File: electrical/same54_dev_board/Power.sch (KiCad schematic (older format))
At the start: 1 part, among them U1 p_ATSAME54P20A-AU

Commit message: Trying to figure out how I want to do power...
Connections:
- net at U1.14 (GNDANA1): now also U1.25 (GNDANA2)
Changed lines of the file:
@@
 Wire Wire Line
 	5800 3450 5800 3550
+Wire Wire Line
+	5800 3800 5800 3900
 $EndSCHEMATC

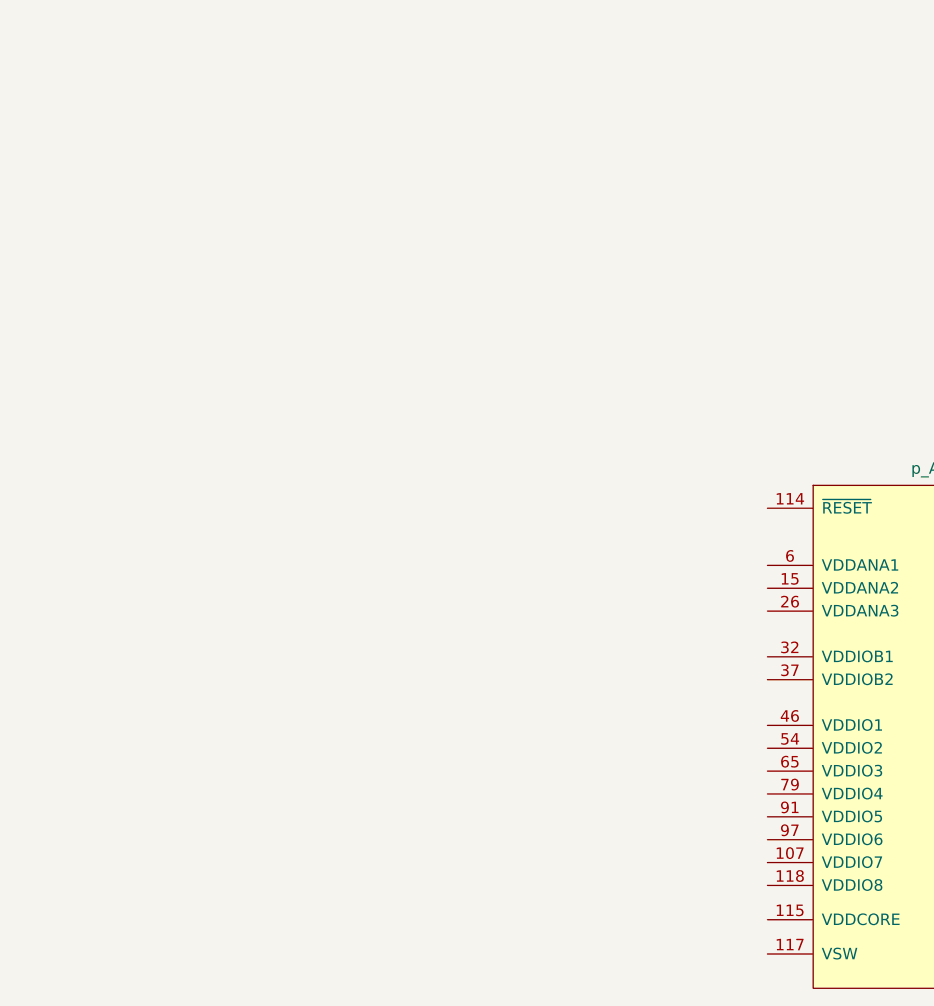
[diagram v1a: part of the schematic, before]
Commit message: going with barrel jack 5v+2A optional input, with usb supplying 400mA + 100mA for internals
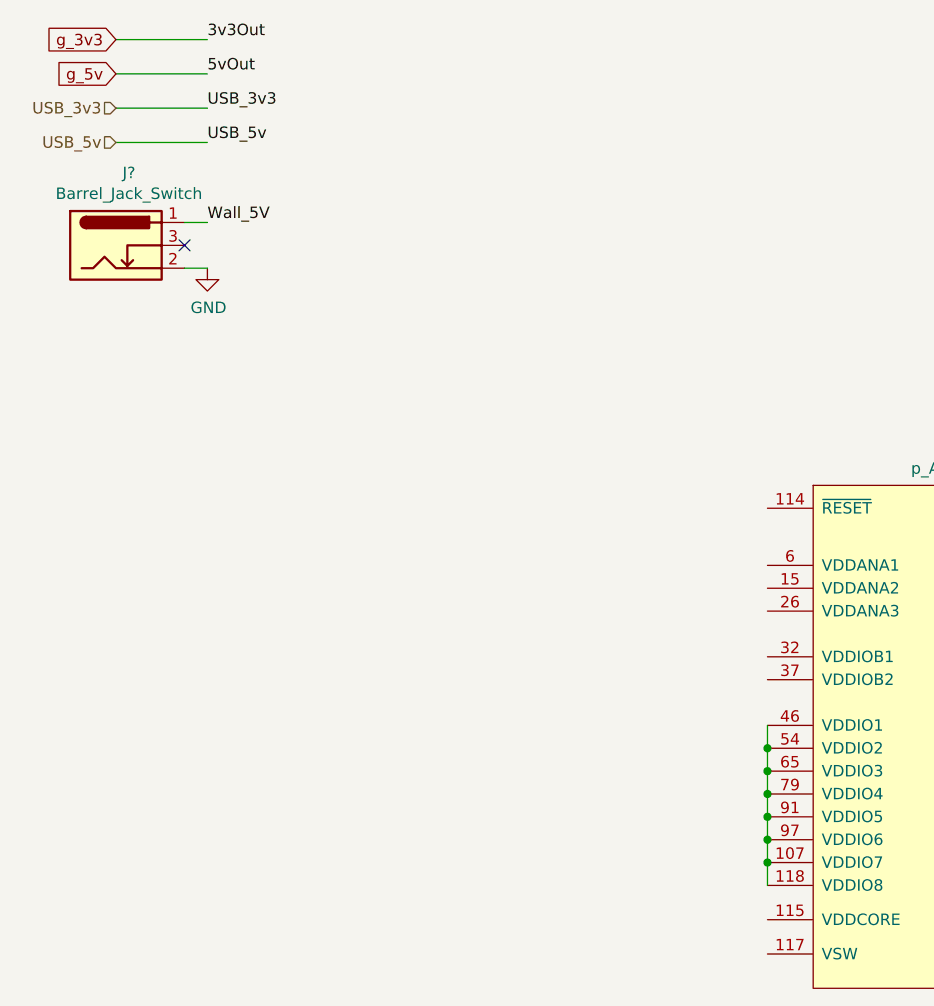
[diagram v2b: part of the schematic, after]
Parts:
- added J?: Barrel_Jack_Switch, symbol Connector:Barrel_Jack_Switch
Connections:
- net at U1.107 (VDDIO7): now also U1.118 (VDDIO8), U1.46 (VDDIO1), U1.54 (VDDIO2), U1.65 (VDDIO3), U1.79 (VDDIO4), U1.91 (VDDIO5), U1.97 (VDDIO6)
- new net GND: J?.2
- new net Wall_5V: J?.1
- no-connect marks 0 -> 1
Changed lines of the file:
@@
 Wire Wire Line
 	5800 3800 5800 3900
+Text HLabel 950  900  0    50   Input ~ 0
+USB_3v3
+Text HLabel 950  1050 0    50   Input ~ 0
+USB_5v
+Text GLabel 950  600  0    50   Input ~ 0
+g_3v3
+Text GLabel 950  750  0    50   Input ~ 0
+g_5v
+Wire Wire Line
+	950  900  1350 900
+Text Label 1350 900  0    50   ~ 0
+USB_3v3
+Wire Wire Line
+	950  1050 1350 1050
+Text Label 1350 1050 0    50   ~ 0
+USB_5v
+Wire Wire Line
+	950  600  1350 600
+Wire Wire Line
+	950  750  1350 750
+Text Label 1350 600  0    50   ~ 0
+3v3Out
+Text Label 1350 750  0    50   ~ 0
+5vOut
+Wire Wire Line
+	3800 3600 3800 3700
+Connection ~ 3800 3700
+Wire Wire Line
+	3800 3700 3800 3800
+Connection ~ 3800 3800
+Wire Wire Line
+	3800 3800 3800 3900
+Connection ~ 3800 3900
+Wire Wire Line
+	3800 3900 3800 4000
+Connection ~ 3800 4000
+Wire Wire Line
+	3800 4000 3800 4100
+Connection ~ 3800 4100
+Wire Wire Line
+	3800 4100 3800 4200
+Connection ~ 3800 4200
+Wire Wire Line
+	3800 4200 3800 4300
+$Comp
+L Connector:Barrel_Jack_Switch J?
+U 1 1 5E88DD8C
+P 950 1500
+F 0 "J?" H 1007 1817 50  0000 C CNN
+F 1 "Barrel_Jack_Switch" H 1007 1726 50  0000 C CNN
+F 2 "" H 1000 1460 50  0001 C CNN
+F 3 "~" H 1000 1460 50  0001 C CNN
+	1    950  1500
+	1    0    0    -1
+$EndComp
+Wire Wire Line
+	1250 1400 1350 1400
+Text Label 1350 1400 0    50   ~ 0
+Wall_5V
+NoConn ~ 1250 1500
+Wire Wire Line
+	1250 1600 1350 1600
+$Comp
+L power:GND #PWR?
+U 1 1 5E8980B4
+P 1350 1600
+F 0 "#PWR?" H 1350 1350 50  0001 C CNN
+F 1 "GND" H 1355 1427 50  0000 C CNN
+F 2 "" H 1350 1600 50  0001 C CNN
+F 3 "" H 1350 1600 50  0001 C CNN
+	1    1350 1600
+	1    0    0    -1
+$EndComp
 $EndSCHEMATC

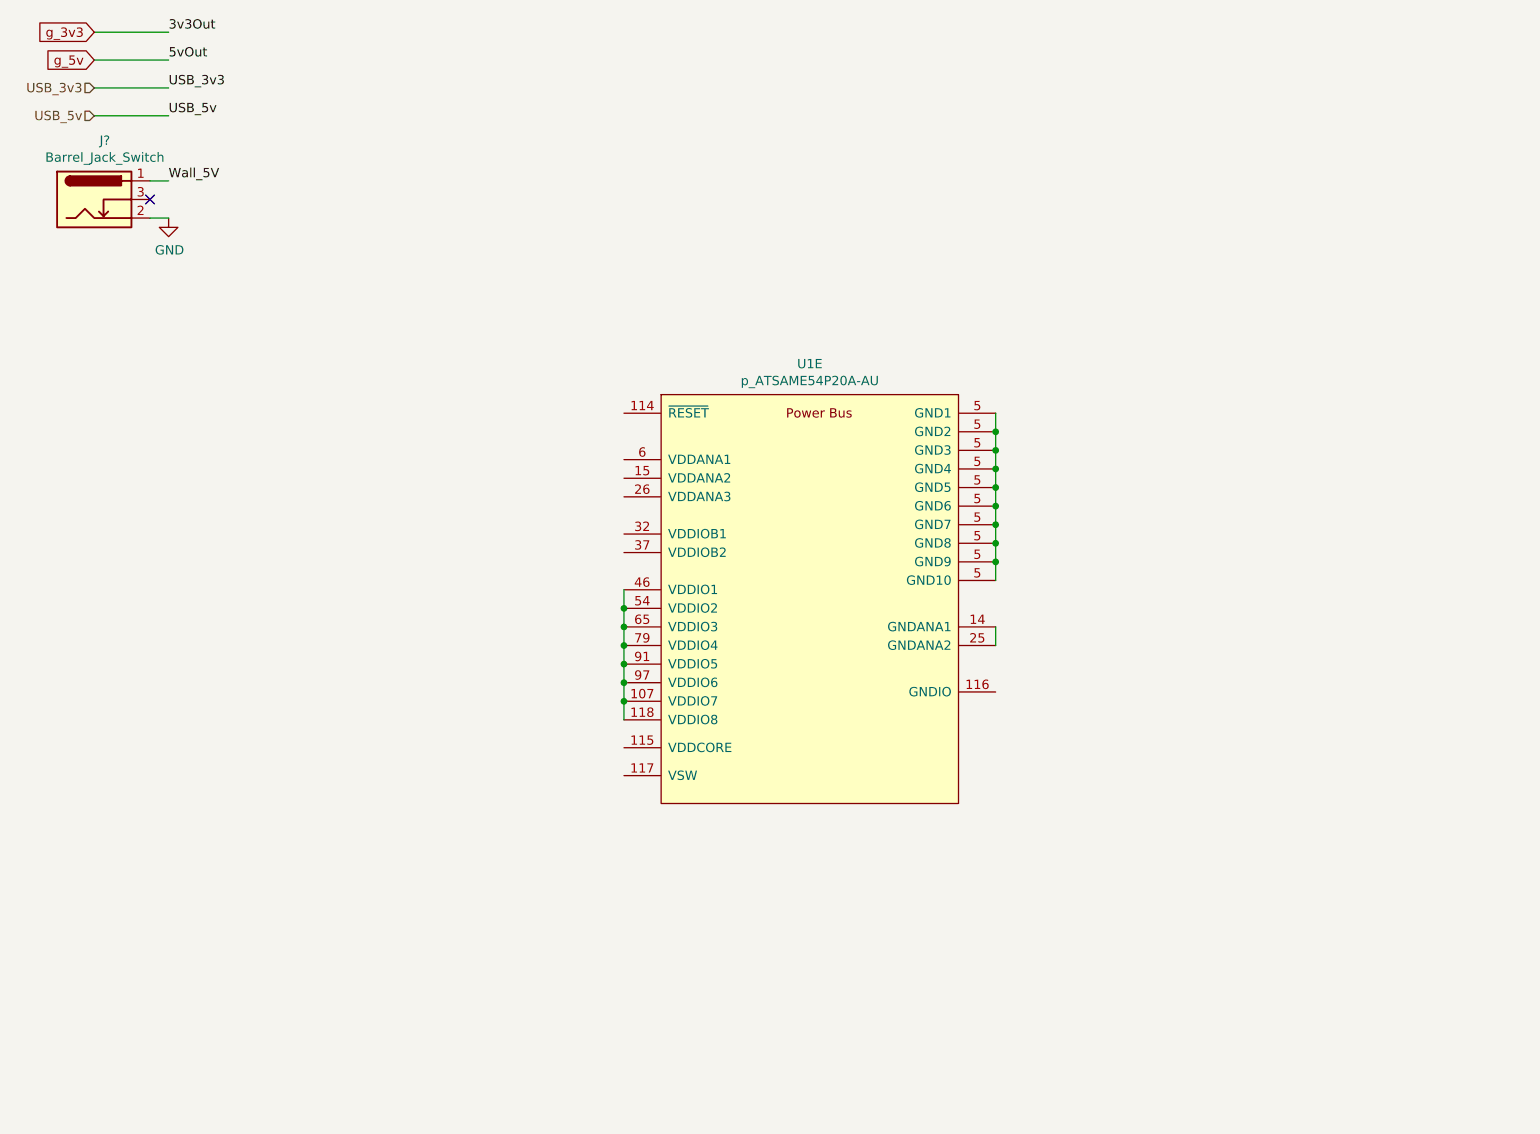
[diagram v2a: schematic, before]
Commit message: Added usart, i2c, and spi pin locations, as well as labeled sercoms
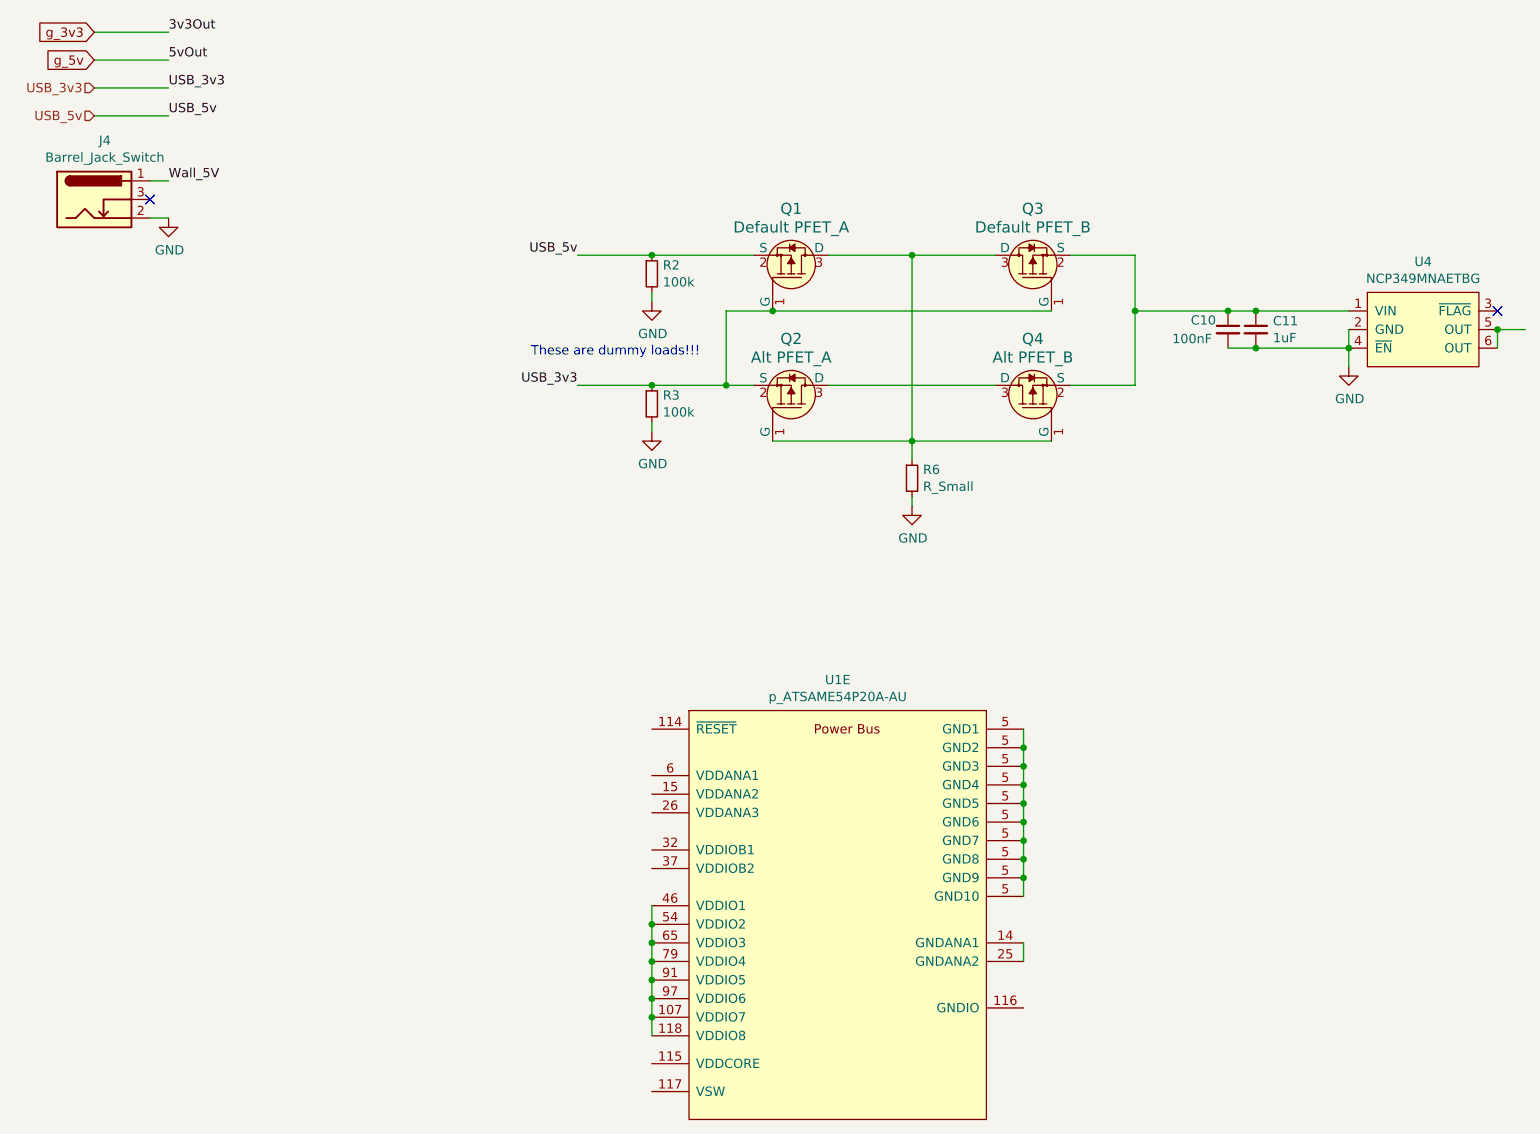
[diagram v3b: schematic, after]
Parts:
- added C10: 100nF, symbol Device:C_Small
- added C11: 1uF, symbol Device:C_Small
- added Q1: Default PFET_A, digikey-footprints:SOT-23-3, symbol dk_Transistors-FETs-MOSFETs-Single:IRLML6402TRPBF
- added Q2: Alt PFET_A, digikey-footprints:SOT-23-3, symbol dk_Transistors-FETs-MOSFETs-Single:IRLML6402TRPBF
- added Q3: Default PFET_B, digikey-footprints:SOT-23-3, symbol dk_Transistors-FETs-MOSFETs-Single:IRLML6402TRPBF
- added Q4: Alt PFET_B, digikey-footprints:SOT-23-3, symbol dk_Transistors-FETs-MOSFETs-Single:IRLML6402TRPBF
- added R2, R3: 100k, symbol Device:R_Small
- added R6: R_Small, symbol Device:R_Small
- added U4: NCP349MNAETBG, Package_DFN_QFN:DFN-6-1EP_2x2mm_P0.65mm_EP1x1.6mm, symbol NCP349MNAETBG:NCP349MNAETBG
- gave numbers to parts that had none: 1
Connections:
- net GND: now also C10.2, C11.2, R2.2, R3.2, R6.2, U4.2 (GND), U4.4 (~EN)
- net USB_3v3: now also Q1.1 (G), Q2.2 (S), Q3.1 (G), R3.1
- net USB_5v: now also Q1.2 (S), R2.1
- new net: C10.1, C11.1, Q3.2 (S), Q4.2 (S), U4.1 (VIN)
- new net: U4.5 (OUT), U4.6 (OUT)
- new net: Q1.3 (D), Q2.1 (G), Q3.3 (D), Q4.1 (G), R6.1
- new net: Q2.3 (D), Q4.3 (D)
- no-connect marks 1 -> 2
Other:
- note added: "These are dummy loads!!!"
- moved on the sheet: U1E

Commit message: Made board smaller, changed some small things
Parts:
- J4: footprint (none) -> digikey-footprints:Barrel_Jack_5.5mmODx2.1mmID_PJ-102A
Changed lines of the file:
@@
 F 0 "J4" H 1007 1817 50  0000 C CNN
 F 1 "Barrel_Jack_Switch" H 1007 1726 50  0000 C CNN
-F 2 "" H 1000 1460 50  0001 C CNN
+F 2 "digikey-footprints:Barrel_Jack_5.5mmODx2.1mmID_PJ-102A" H 1000 1460 50  0001 C CNN
 F 3 "~" H 1000 1460 50  0001 C CNN
 	1    950  1500

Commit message: migrating to laptop
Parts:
- U4: symbol NCP349MNAETBG:NCP349MNAETBG -> same54_dev_board-rescue:NCP349MNAETBG-NCP349MNAETBG
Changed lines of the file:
@@
 	4900 1800 5350 1800
 $Comp
-L NCP349MNAETBG:NCP349MNAETBG U4
+L same54_dev_board-rescue:NCP349MNAETBG-NCP349MNAETBG U4
 U 1 1 5E7F2428
 P 8100 2250
+AR Path="/5E7F2428" Ref="U4"  Part="1"
+AR Path="/5E7872D3/5E7F2428" Ref="U4"  Part="1"
 F 0 "U4" H 8100 2665 50  0000 C CNN
 F 1 "NCP349MNAETBG" H 8100 2574 50  0000 C CNN
